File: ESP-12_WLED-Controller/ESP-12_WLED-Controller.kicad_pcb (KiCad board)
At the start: 2 copper layers, 58.7 x 31.1 mm, 26 parts, among them J1 Conn_01x02_Male, J2 Conn_01x04_Male, J3 Conn_01x03_Male, Q1 2N7000, SW1 SW_RST, U1 TS1117-3.3, U2 ESP-12E, U3 SN74LVC1T45DBV

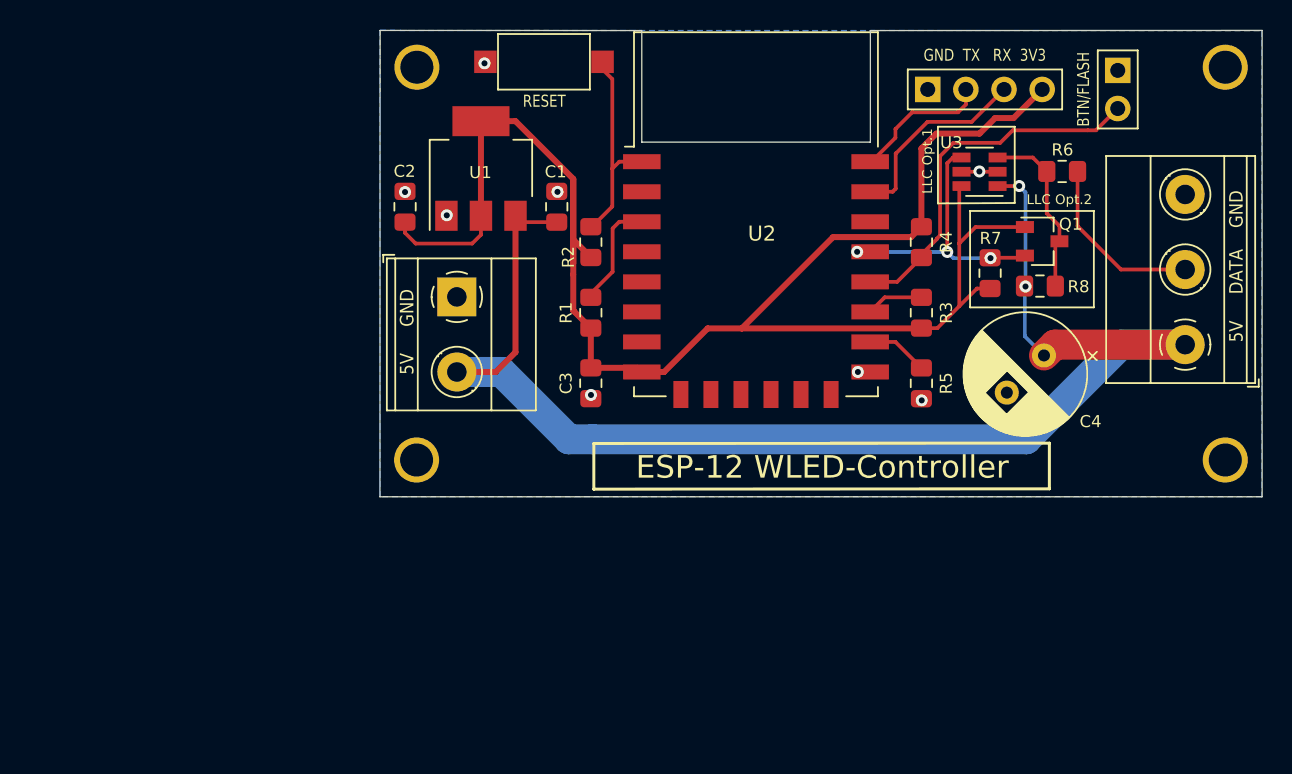
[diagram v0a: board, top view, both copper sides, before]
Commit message: add IRF7410 Power MOSFET
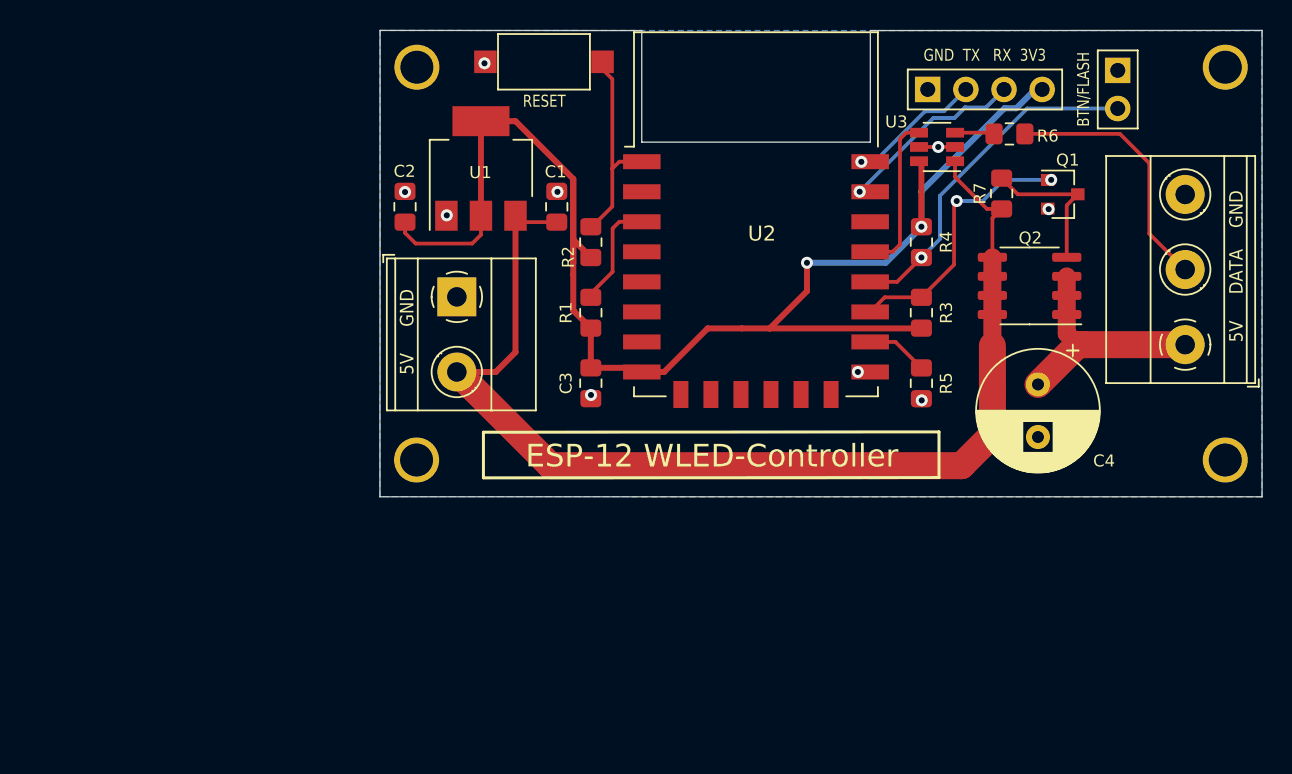
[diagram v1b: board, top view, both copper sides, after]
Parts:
- removed R8: 10k, Resistor_SMD:R_0805_2012Metric_Pad1.15x1.40mm_HandSolder
- added Q2: IRF7404, Package_SO:SOIC-8_3.9x4.9mm_P1.27mm, F.Cu at (185.7, 88.0)
- Q1: value 2N7000 -> BC847
- moved R7 5.36 mm to (183.9, 81.8)
- moved R6 4.31 mm to (184.4, 77.8)
- moved G*** 4.00 mm to (172.2, 93.3)
- moved Q1 3.42 mm to (187.9, 81.9)
- moved U3 3.28 mm to (179.6, 78.7)
- moved C4 1.97 mm to (186.3, 94.5), turned to 270 degrees
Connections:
- C4 pad 1: +5V -> WS-Strip
- J3 pad 1: +5V -> WS-Strip
- Q1 pad 1: GPIO4_3.3 -> /GPIO2
- Q1 pad 2: +3V3 -> GND
- Q1 pad 3: GPIO4_5 -> Net-(Q1-Pad3)
- R7 pad 1: +3V3 -> +5V
- R7 pad 2: GPIO4_3.3 -> Net-(Q1-Pad3)
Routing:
- net +3V3: track 128.8 -> 111.3 mm, vias 0 -> 2
- net +5V: track 92.6 -> 75.9 mm, vias 2 -> 0
- net WS-Strip: track 0.00 -> 15.7 mm
- net /GPIO2: track 3.82 -> 18.1 mm, vias 0 -> 2
- net Net-(Q1-Pad3): track 0.00 -> 10.0 mm
- net GPIO4_5: track 11.7 -> 2.63 mm
- net GPIO4_3.3: track 18.7 -> 10.7 mm, vias 3 -> 0
- net Net-(J3-Pad2): track 12.1 -> 17.3 mm
- net /GPIO0: track 24.5 -> 23.0 mm, vias 0 -> 1
- net RX: track 13.1 -> 12.4 mm, vias 0 -> 1
- net TX: track 9.29 -> 8.96 mm, vias 0 -> 1
- net GND: track 2.20 -> 2.40 mm, vias 8 -> 9
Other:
- board text removed: "LLC Opt.1"
- board text removed: "LLC Opt.2"

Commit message: LLC changes
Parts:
- removed U3: SN74LVC1T45DBV, Package_TO_SOT_SMD:SOT-23-6
- added D1: SS14, Diode_SMD:D_SMA_Handsoldering, F.Cu at (188.7, 81.8)
- added R8: 10k, Resistor_SMD:R_0805_2012Metric_Pad1.15x1.40mm_HandSolder, F.Cu at (184.0, 83.8)
- added U4: 74LVC1G125, Package_SO:TSOP-5_1.65x3.05mm_P0.95mm, F.Cu at (178.9, 77.9)
- added altQ2: alt. MOSFET, Package_TO_SOT_THT:TO-220-3_Vertical, F.Cu at (187.1, 90.1)
- Q1: value BC847 -> TSM2302CX
- Q2: value IRF7404 -> IRF7410
- moved C4 5.51 mm to (191.7, 95.7)
- moved R7 4.44 mm to (179.4, 81.9), turned to 180 degrees
- moved Q1 4.19 mm to (184.0, 80.4), turned to 90 degrees
- moved Q2 2.42 mm to (184.6, 90.1), turned to 90 degrees
- moved J3 1.98 mm to (196.1, 89.9)
- moved JP1 1.69 mm to (193.2, 74.0), turned to 270 degrees
- moved J2 0.87 mm to (178.9, 74.0)
- moved R6 0.71 mm to (184.0, 77.2)
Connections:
- C4 pad 1: WS-Strip -> WS-Strip_VCC
- J3 pad 1: WS-Strip -> WS-Strip_VCC
- Q1 pad 1: /GPIO2 -> GPIO12
- Q2 pad 1: WS-Strip -> +5V
- Q2 pad 2: WS-Strip -> +5V
- Q2 pad 3: WS-Strip -> +5V
- Q2 pad 5: +5V -> WS-Strip_VCC
- Q2 pad 6: +5V -> WS-Strip_VCC
- Q2 pad 7: +5V -> WS-Strip_VCC
- Q2 pad 8: +5V -> WS-Strip_VCC
- R3 pad 2: /GPIO2 -> GPIO2
- U2 pad 17: /GPIO2 -> GPIO2
- U2 pad 6: Net-(U2-Pad6) -> GPIO12
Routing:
- net GPIO12: track 0.00 -> 28.5 mm
- net WS-Strip_VCC: track 0.00 -> 28.0 mm
- net /GPIO2: track 18.1 -> 0.00 mm, vias 2 -> 0
- net GND: track 2.40 -> 18.7 mm, vias 9 -> 8
- net WS-Strip: track 15.7 -> 0.00 mm
- net Net-(Q1-Pad3): track 10.0 -> 24.4 mm, vias 0 -> 1
- net +5V: track 75.9 -> 86.9 mm, vias 0 -> 1
- net Net-(J3-Pad2): track 17.3 -> 27.7 mm
- net GPIO2: track 0.00 -> 3.83 mm
- net /GPIO0: track 23.0 -> 25.8 mm
- net +3V3: track 111.3 -> 108.9 mm
- net GPIO4_3.3: track 10.7 -> 9.49 mm

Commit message: some changes
single Terminal-Block
parts clean up
edit footprints for handsolder
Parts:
- removed J3: Conn_01x03_Male, TerminalBlock_Phoenix:TerminalBlock_Phoenix_MKDS-1,5-3_1x03_P5.00mm_Horizontal
- J1: value Conn_01x02_Male -> Conn_01x04_Male; footprint TerminalBlock_Phoenix:TerminalBlock_Phoenix_MKDS-1,5-2_1x02_P5.00mm_Horizontal -> TerminalBlock_Phoenix:TerminalBlock_Phoenix_MKDS-1,5-4-5.08_1x04_P5.08mm_Horizontal
- moved JP1 49.1 mm to (146.9, 90.3), turned to 0 degrees
- moved J1 48.7 mm to (196.1, 94.1), turned to 90 degrees
- moved J2 30.7 mm to (151.4, 87.7), turned to 0 degrees
- moved R6 6.56 mm to (189.1, 73.0)
- moved U4 5.98 mm to (183.3, 73.9)
- moved R8 5.43 mm to (179.5, 80.8)
- moved C4 5.13 mm to (186.9, 97.6), turned to 180 degrees
- moved altQ2 4.78 mm to (182.4, 89.1), turned to 0 degrees
- moved R7 4.08 mm to (179.5, 77.8)
- moved D1 1.52 mm to (188.4, 80.3)
- moved G*** 1.20 mm to (172.2, 92.1)
- moved Q1 1.08 mm to (183.7, 81.4)
- moved Q2 1.04 mm to (184.9, 89.1), turned to 270 degrees
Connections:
- net GPIO12 renamed RELAY
- J1 pad 1: GND -> WS-Strip_VCC
- R6 pad 1: Net-(J3-Pad2) -> Net-(J1-Pad3)
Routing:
- net +5V: track 86.9 -> 118.3 mm, vias 1 -> 4
- net Net-(J3-Pad2): track 27.7 -> 0.00 mm
- net +3V3: track 108.9 -> 82.6 mm, vias 2 -> 0
- net TX: track 9.27 -> 28.1 mm
- net Net-(J1-Pad3): track 0.00 -> 17.7 mm
- net RX: track 12.7 -> 28.3 mm
- net /GPIO0: track 25.8 -> 40.0 mm, vias 1 -> 2
- net WS-Strip_VCC: track 28.0 -> 41.9 mm, vias 0 -> 4
- net GPIO4_3.3: track 9.49 -> 19.3 mm, vias 0 -> 2
- net Net-(Q1-Pad3): track 24.4 -> 15.7 mm, vias 1 -> 0
- net GND: track 18.7 -> 14.5 mm, vias 8 -> 10
- net /Reset: track 14.2 -> 18.0 mm
- net GPIO4_5: track 3.12 -> 3.93 mm
- net RELAY: track 28.5 -> 29.1 mm
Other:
- board text added: "3V3 TX RX GND"
- board text added: "GND DATA 5V SW_5V"
- board text added: "GND RX TX 3V3"
- board text added: "SW_5V 5V DATA GND"
- board text removed: "3V3 RX TX GND"
- board text removed: "5V DATA GND"
- board text removed: "5V GND"
- board text removed: "GND 5V"
- board text removed: "GND DATA 5V"
- board text removed: "GND TX RX 3V3"

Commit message: some PCB updates
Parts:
- removed the REF** at (198.8, 99.6)
- removed the REF** at (144.9, 73.4)
- removed the REF** at (144.9, 99.6)
- removed the REF** at (198.8, 73.4)
- added REF**: MountingHole_2.2mm_M2_Pad_Via, MountingHole:MountingHole_2.2mm_M2_Pad_Via, F.Cu at (175.4, 89.9)
- added REF**: MountingHole_2.2mm_M2_Pad_Via, MountingHole:MountingHole_2.2mm_M2_Pad_Via, F.Cu at (175.4, 115.9)
- added REF**: MountingHole_2.2mm_M2_Pad_Via, MountingHole:MountingHole_2.2mm_M2_Pad_Via, F.Cu at (121.8, 115.9)
- added REF**: MountingHole_2.2mm_M2_Pad_Via, MountingHole:MountingHole_2.2mm_M2_Pad_Via, F.Cu at (121.8, 89.9)
- moved D1 29.1 mm to (164.4, 96.7)
- moved C4 28.5 mm to (163.6, 114.0)
- moved R1 28.5 mm to (133.2, 106.2)
- moved R3 28.5 mm to (155.3, 106.2)
- moved R7 28.5 mm to (156.2, 94.2)
- moved C1 28.5 mm to (131.0, 99.1)
- moved C2 28.5 mm to (120.9, 99.1)
- moved C3 28.5 mm to (133.2, 110.9)
- moved G*** 28.5 mm to (148.9, 108.5)
- moved J2 28.5 mm to (128.2, 104.1)
- moved Q1 28.5 mm to (160.4, 97.8)
- moved Q2 28.5 mm to (161.7, 105.5)
- moved R2 28.5 mm to (133.2, 101.5)
- moved R4 28.5 mm to (155.3, 101.5)
- moved R5 28.5 mm to (155.3, 110.9)
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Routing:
- net Net-(J1-Pad3): track 17.7 -> 28.1 mm
- net +5V: track 118.3 -> 124.5 mm
- net WS-Strip_VCC: track 41.9 -> 46.6 mm
- net GND: track 14.5 -> 18.8 mm
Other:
- outline, holes or cut-outs redrawn

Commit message: Update to V1.0
clean schematic
add description
TX <-> RX
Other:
- board text added: "V1.0 - 07/2021 - P.Wulfert"
- board text removed: "V0.9 - 06/2021 - P.Wulfert"

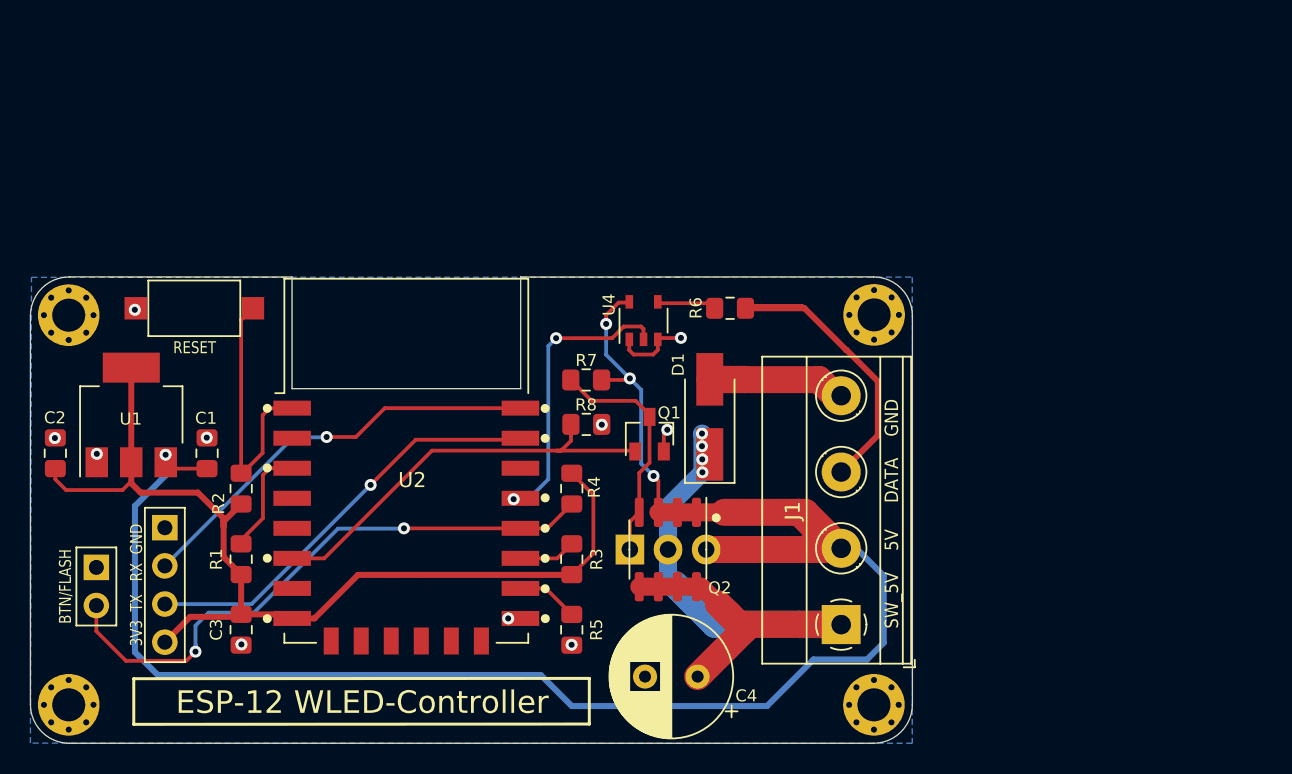
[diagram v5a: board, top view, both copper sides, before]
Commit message: Upgrade to V1.1
Added R9 gate resistor to PCB
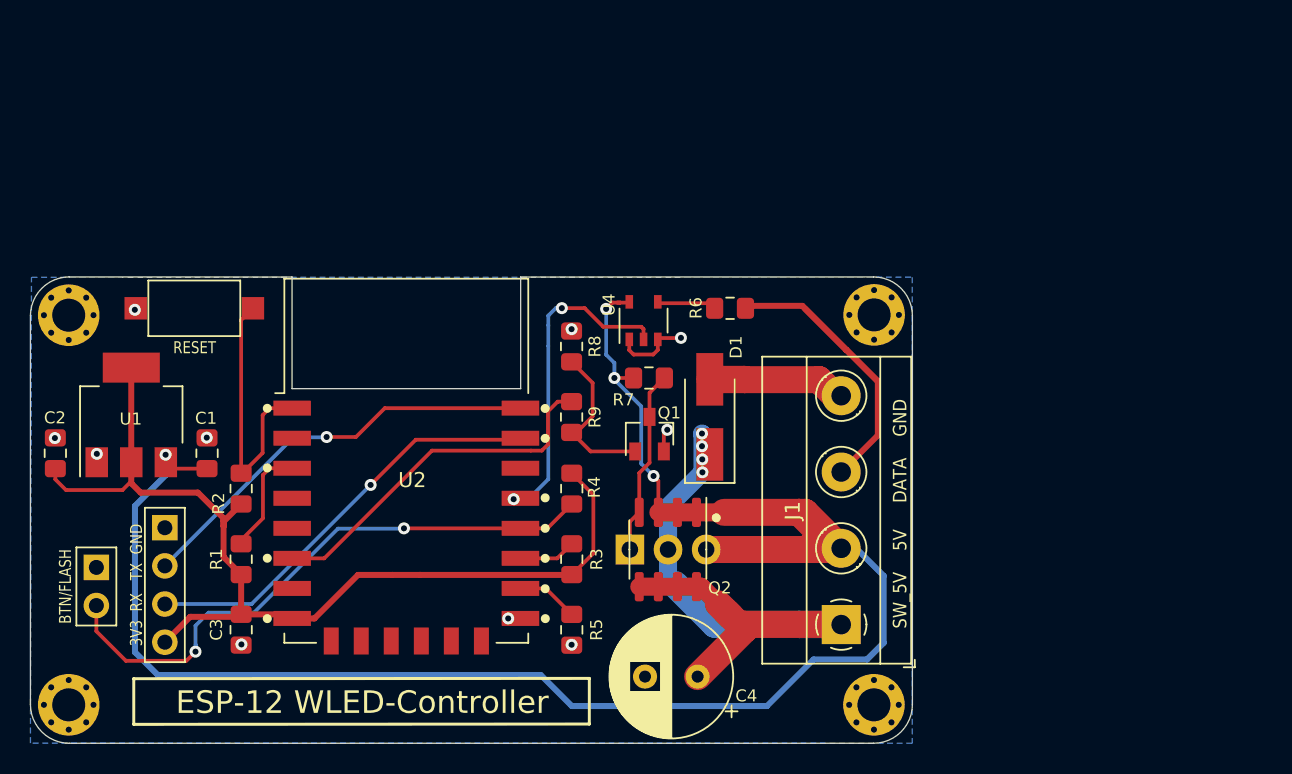
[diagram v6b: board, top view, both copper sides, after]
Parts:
- added R9: 100R, Resistor_SMD:R_0805_2012Metric_Pad1.15x1.40mm_HandSolder, F.Cu at (155.2, 96.7)
- C3: value C -> 100nF
- D1: value SS14 -> Flyback diode
- Q1: value TSM2302CX -> IRLML6344
- R6: value 330R -> 470R
- moved R8 5.28 mm to (155.2, 92.0), turned to 90 degrees
- moved R7 4.18 mm to (160.4, 94.1), turned to 0 degrees
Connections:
- Q1 pad 1: RELAY -> Net-(Q1-Pad1)
- R8 pad 1: RELAY -> Net-(Q1-Pad1)
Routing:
- net Net-(Q1-Pad1): track 0.00 -> 10.9 mm
- net Net-(J1-Pad3): track 28.1 -> 35.2 mm
- net RELAY: track 29.1 -> 24.2 mm
- net Net-(Q1-Pad3): track 15.7 -> 12.5 mm
- net GPIO4_3.3: track 19.3 -> 21.5 mm
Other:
- board text added: "3V3 RX TX GND"
- board text added: "GND TX RX 3V3"
- board text added: "V1.1 - 12/2021 - P.Wulfert"
- board text removed: "3V3 TX RX GND"
- board text removed: "GND RX TX 3V3"
- board text removed: "V1.0 - 07/2021 - P.Wulfert"
